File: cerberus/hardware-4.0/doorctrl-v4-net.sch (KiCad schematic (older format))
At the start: 36 parts, among them CON6 RJHSE-5085, U4 ENC28J60, U5 MC34063, X2 25MHz

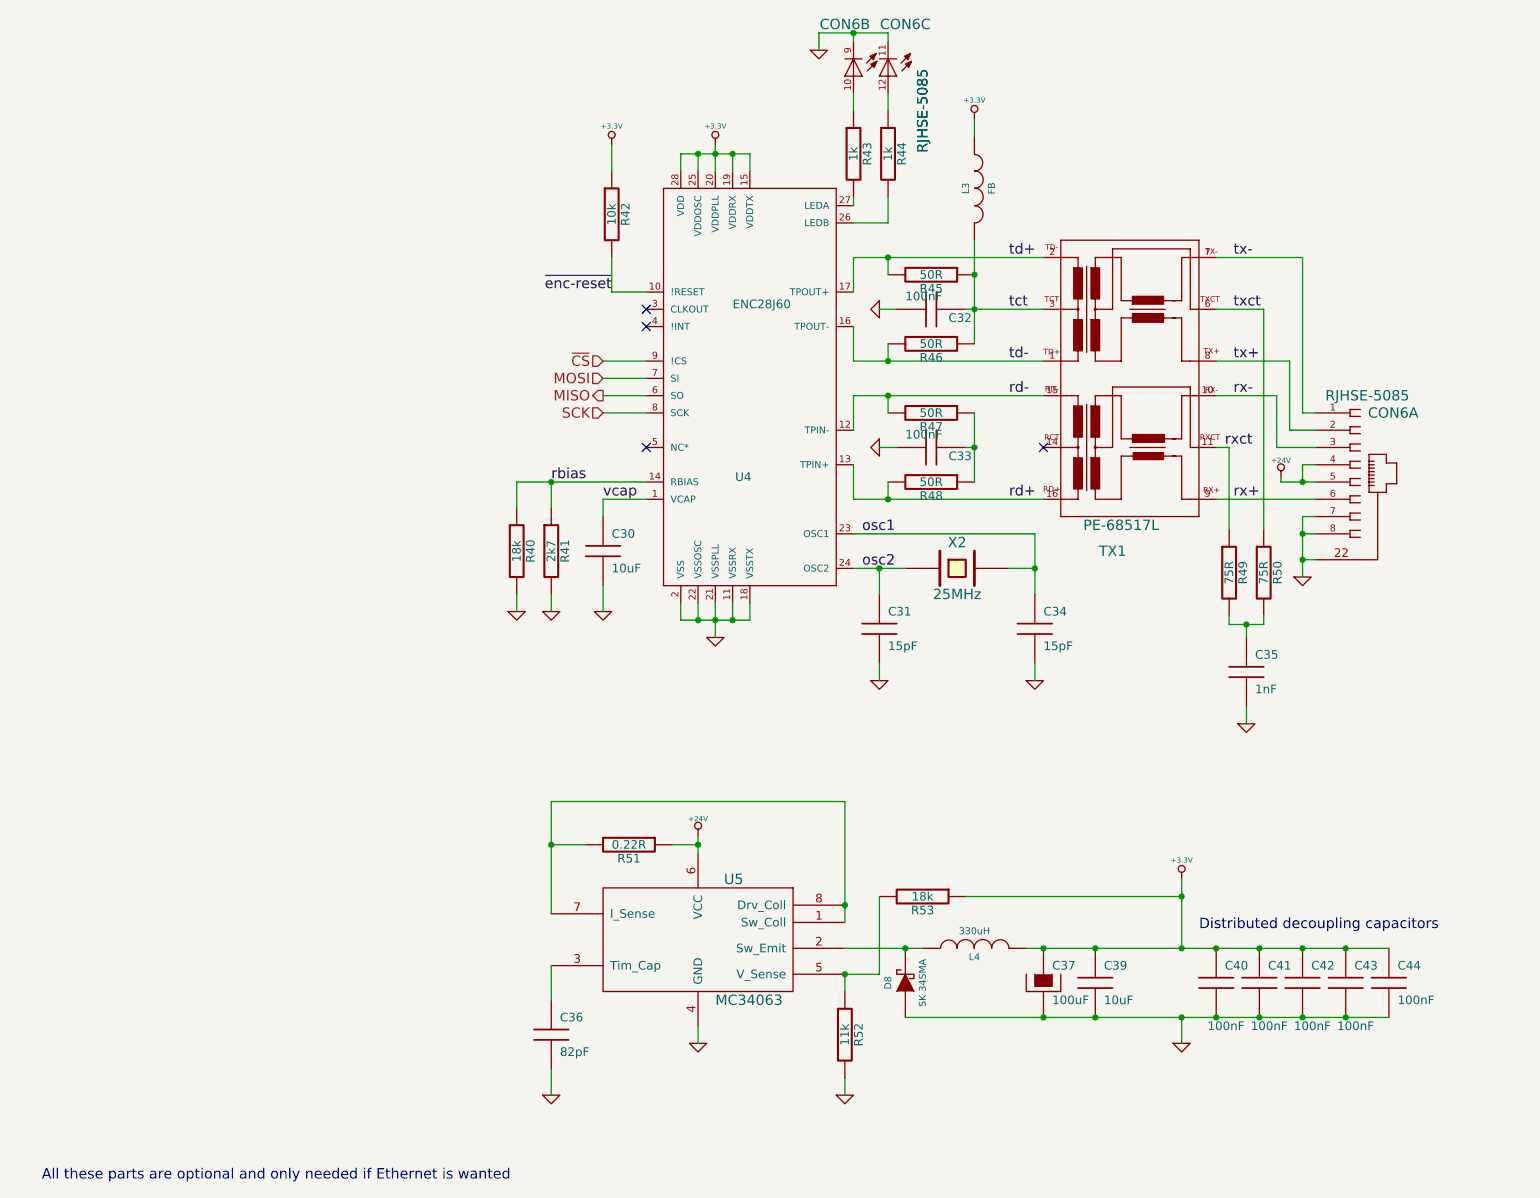
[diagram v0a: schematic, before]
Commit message: Added npn/pnp level shifter for the 3v3 to 5v conversion
git-svn-id: file:///home/ff/projects/osaa/svn@240 a092026d-3e22-4cff-94a7-eaa6fdd35d37
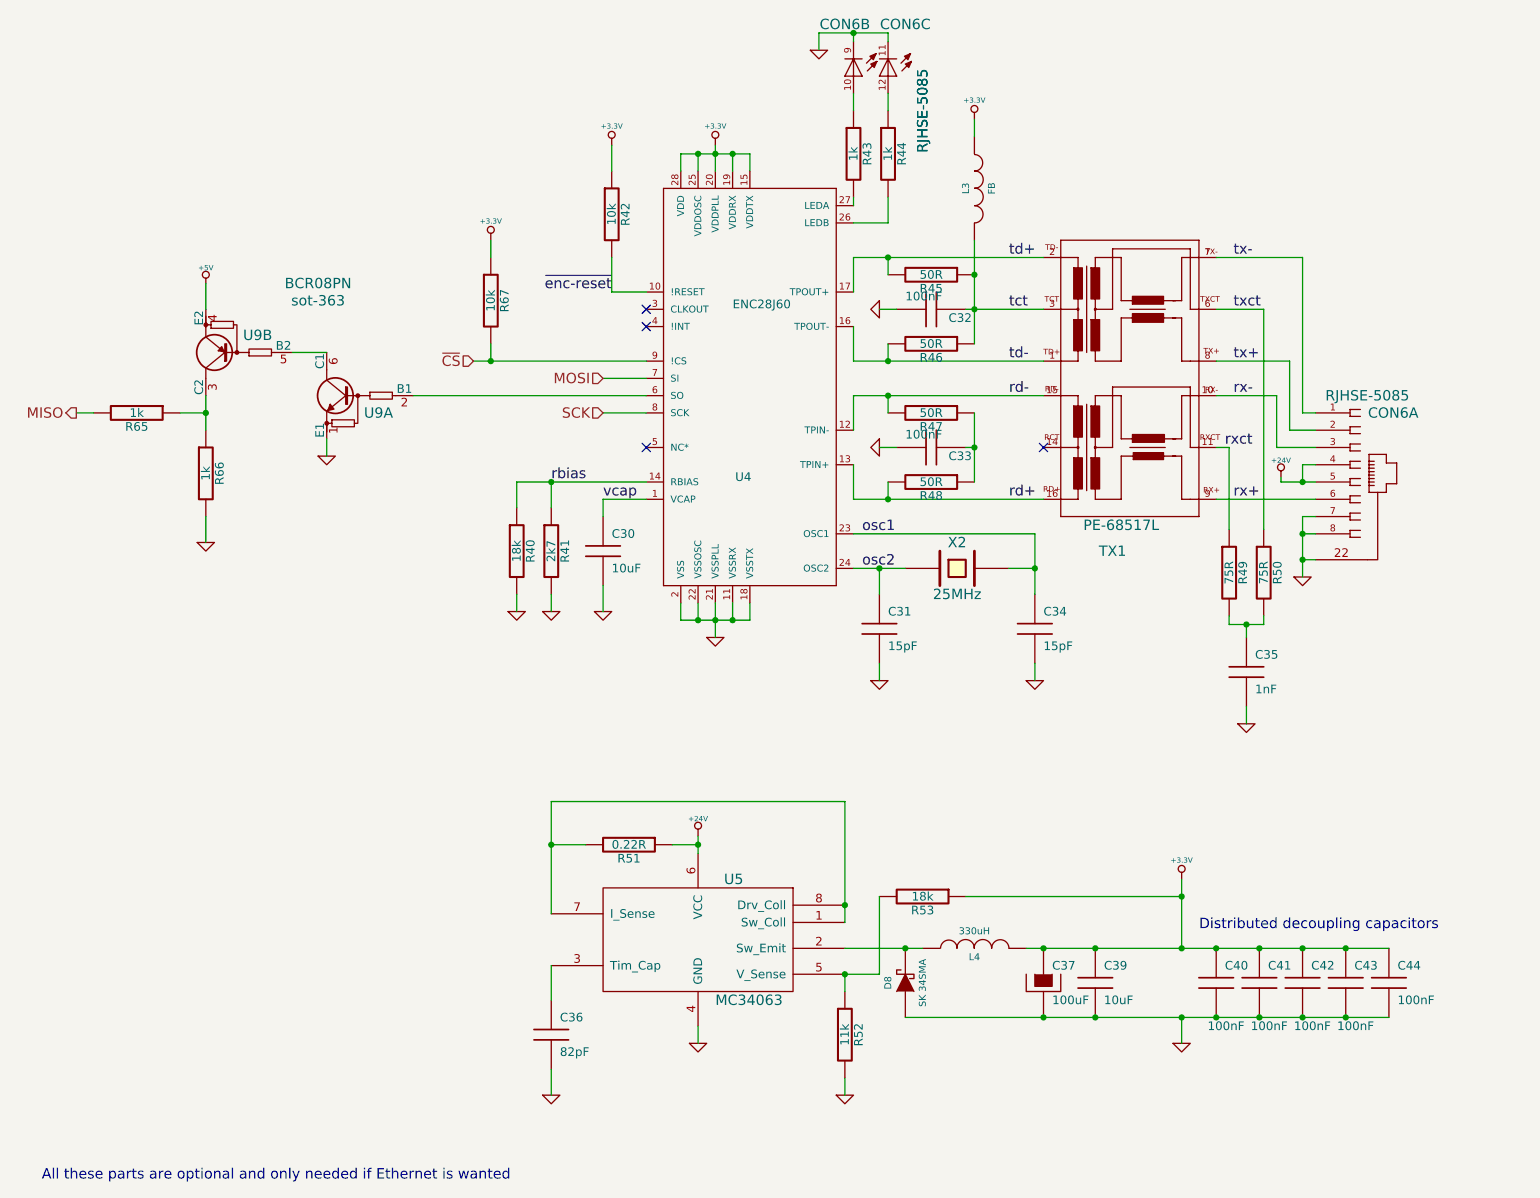
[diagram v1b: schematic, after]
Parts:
- added R65, R66: 1k, symbol R
- added R67: 10k, symbol R
- added U9: BCR08PN, sot-363, symbol NPN/PNP
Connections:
- net +3.3V: now also R67.1
- net GND: now also R66.2, U9.1 (E1)
- net MISO: now also R65.2; no longer U4.6 (SO)
- net ~CS: now also R67.2
- new net: U4.6 (SO), U9.2 (B1)
- new net: R65.1, R66.1, U9.3 (C2)
- new net: U9.5 (B2), U9.6 (C1)
- new net +5V: U9.4 (E2)
